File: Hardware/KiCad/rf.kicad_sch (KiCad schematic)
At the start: 29 parts, among them J8 Conn_Coaxial, U4 CC1200, Y3 40 MHz

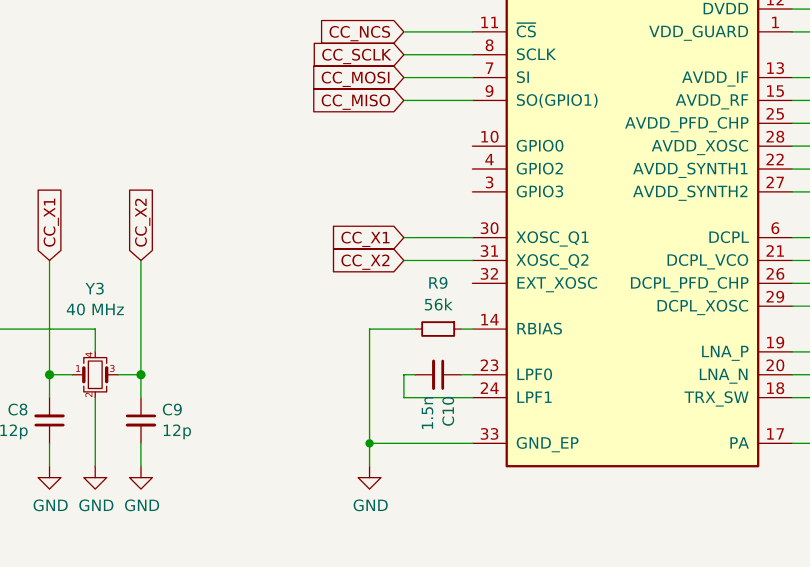
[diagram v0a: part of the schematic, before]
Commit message: Add decoupling capacitors and fix issue #7
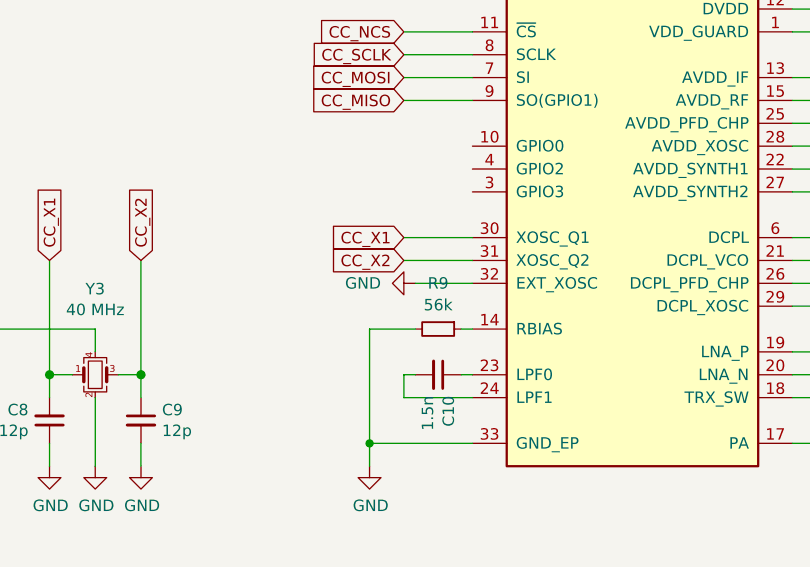
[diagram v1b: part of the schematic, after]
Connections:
- net GND: now also U4.32 (EXT_XOSC)
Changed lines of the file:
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@@
+    (stroke (width 0) (type default) (color 0 0 0 0))
+  )
+  (wire (pts (xy 86.36 63.5) (xy 92.71 63.5))
     (stroke (width 0) (type default) (color 0 0 0 0))
   )
@@
       (effects (font (size 1.27 1.27)) hide)
     )
+    (pin "1")
+  )
+  (symbol (lib_id "power:GND") (at 86.36 63.5 270) (unit 1)
+    (in_bom yes) (on_board yes) (fields_autoplaced)
+    (property "Reference" "#PWR014" (id 0) (at 80.01 63.5 0)
+      (effects (font (size 1.27 1.27)) hide)
+    )
+    (property "Value" "GND" (id 1) (at 82.55 63.4999 90)
+      (effects (font (size 1.27 1.27)) (justify right))
+    )
+    (property "Footprint" "" (id 2) (at 86.36 63.5 0)
+      (effects (font (size 1.27 1.27)) hide)
+    )
+    (property "Datasheet" "" (id 3) (at 86.36 63.5 0)
+      (effects (font (size 1.27 1.27)) hide)
+    )

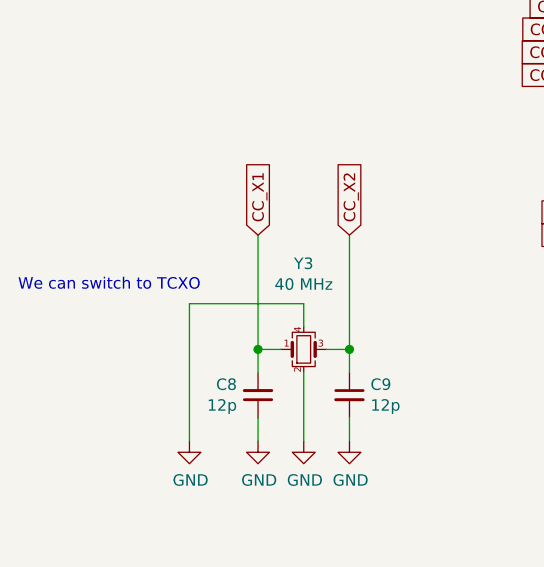
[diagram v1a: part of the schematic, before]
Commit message: Added footprints for decoupling caps
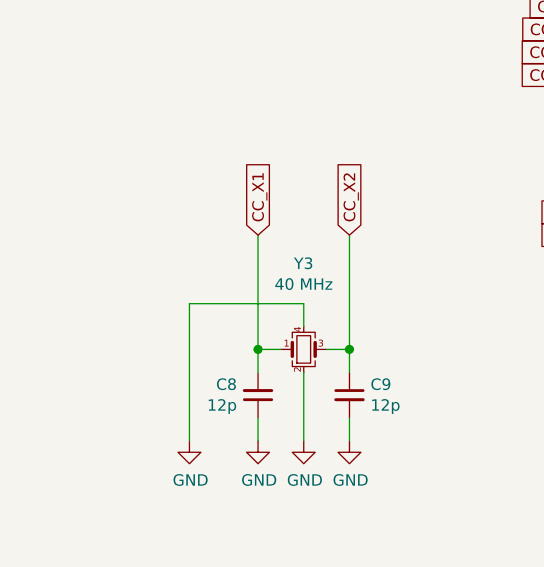
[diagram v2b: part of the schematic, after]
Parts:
- J8: footprint (none) -> Connector_Coaxial:SMA_Amphenol_901-143_Horizontal
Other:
- note removed: "We can switch to TCXO"
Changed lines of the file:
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@@
     (stroke (width 0) (type default) (color 0 0 0 0))
-  )
-  (text "We can switch to TCXO" (at 19.05 67.31 0)
-    (effects (font (size 1.27 1.27)) (justify left bottom))
   )
   (text "Add 9 (?) caps here" (at 139.7 26.67 0)
@@
       (effects (font (size 1.27 1.27)) (justify left))
     )
-    (property "Footprint" "" (id 2) (at 148.59 132.08 0)
-      (effects (font (size 1.27 1.27)) hide)
-    )
+    (property "Footprint" "Connector_Coaxial:SMA_Amphenol_901-143_Horizontal" (id 2) (at 148.59 132.08 0)
+      (effects (font (size 1.27 1.27)) hide)
+    )

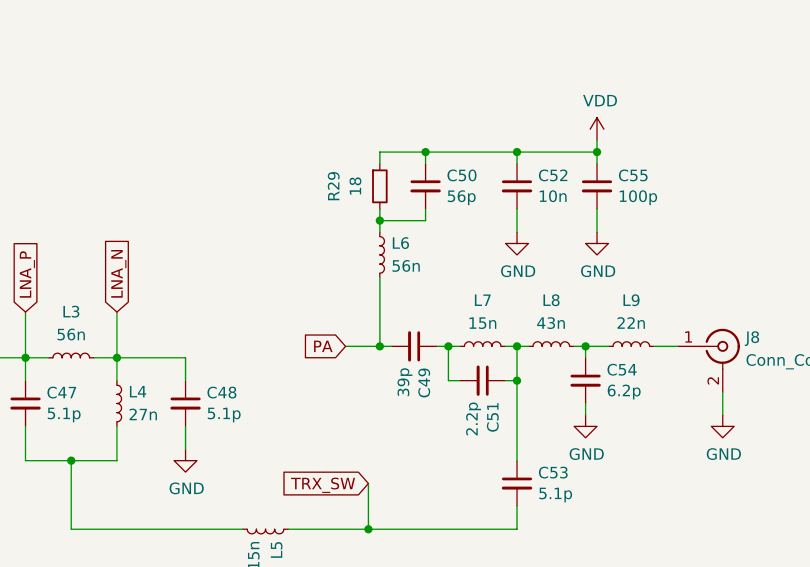
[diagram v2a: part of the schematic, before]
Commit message: Connected SD card to the micro
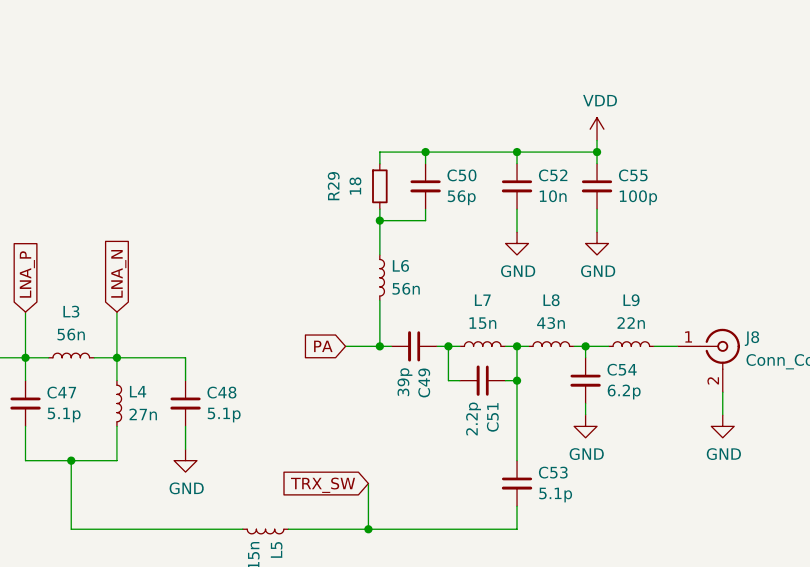
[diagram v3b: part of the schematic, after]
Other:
- moved on the sheet: L6
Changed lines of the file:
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@@
     (stroke (width 0) (type default) (color 0 0 0 0))
   )
-  (wire (pts (xy 110.49 124.46) (xy 110.49 132.08))
+  (wire (pts (xy 110.49 127) (xy 110.49 132.08))
     (stroke (width 0) (type default) (color 0 0 0 0))
   )
@@
     (stroke (width 0) (type default) (color 0 0 0 0))
   )
-  (wire (pts (xy 110.49 118.11) (xy 110.49 119.38))
+  (wire (pts (xy 110.49 118.11) (xy 110.49 121.92))
     (stroke (width 0) (type default) (color 0 0 0 0))
   )
@@
     (pin "1")
   )
-  (symbol (lib_id "Device:L_Small") (at 110.49 121.92 0) (unit 1)
+  (symbol (lib_id "Device:L_Small") (at 110.49 124.46 0) (unit 1)
     (in_bom yes) (on_board yes) (fields_autoplaced)
-    (property "Reference" "L6" (id 0) (at 111.76 120.6499 0)
-      (effects (font (size 1.27 1.27)) (justify left))
-    )
-    (property "Value" "56n" (id 1) (at 111.76 123.1899 0)
-      (effects (font (size 1.27 1.27)) (justify left))
-    )
-    (property "Footprint" "Inductor_SMD:L_0402_1005Metric" (id 2) (at 110.49 121.92 0)
-      (effects (font (size 1.27 1.27)) hide)
-    )
-    (property "Datasheet" "~" (id 3) (at 110.49 121.92 0)
-      (effects (font (size 1.27 1.27)) hide)
-    )
+    (property "Reference" "L6" (id 0) (at 111.76 123.1899 0)
+      (effects (font (size 1.27 1.27)) (justify left))
+    )
+    (property "Value" "56n" (id 1) (at 111.76 125.7299 0)
+      (effects (font (size 1.27 1.27)) (justify left))
+    )
+    (property "Footprint" "Inductor_SMD:L_0402_1005Metric" (id 2) (at 110.49 124.46 0)
+      (effects (font (size 1.27 1.27)) hide)
+    )
+    (property "Datasheet" "~" (id 3) (at 110.49 124.46 0)
+      (effects (font (size 1.27 1.27)) hide)
+    )

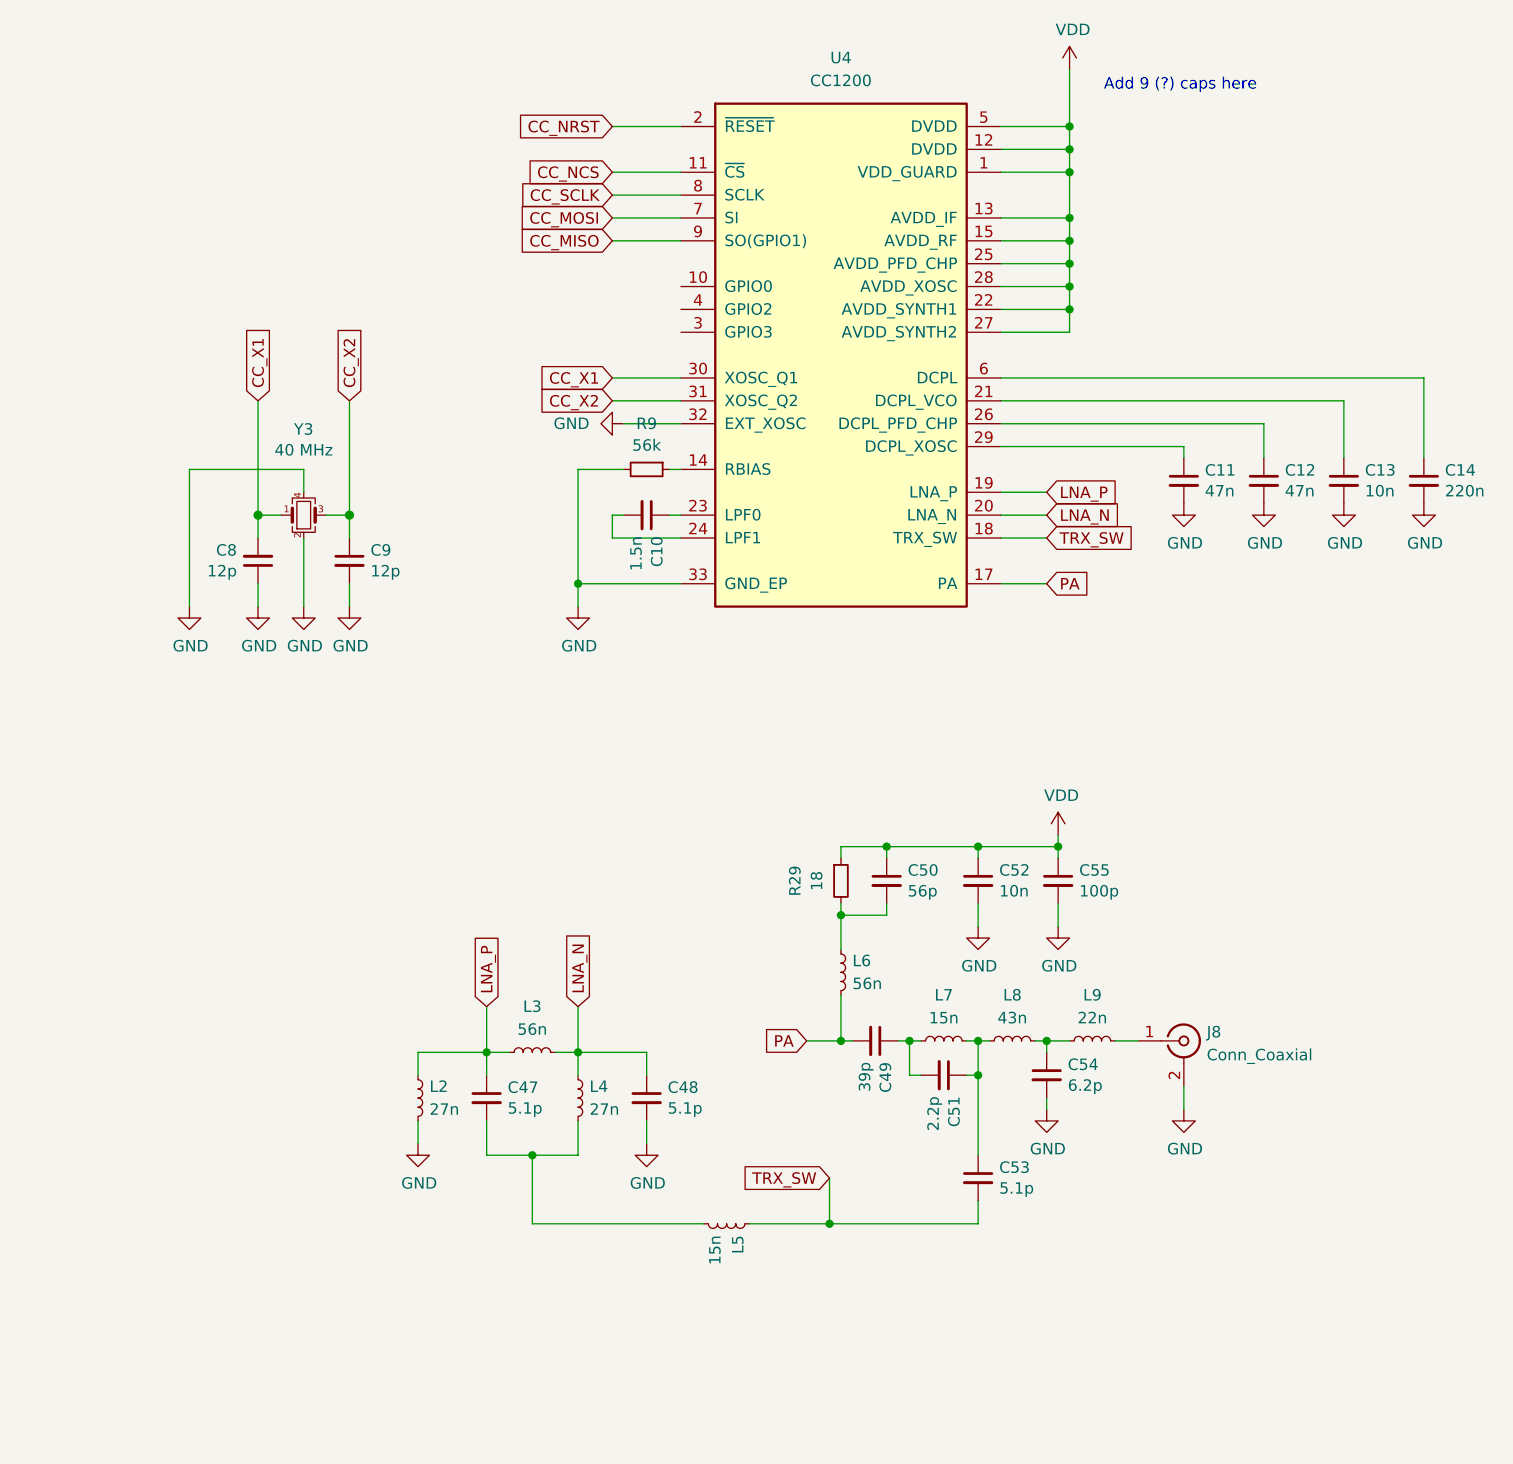
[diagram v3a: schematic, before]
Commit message: Added some connections
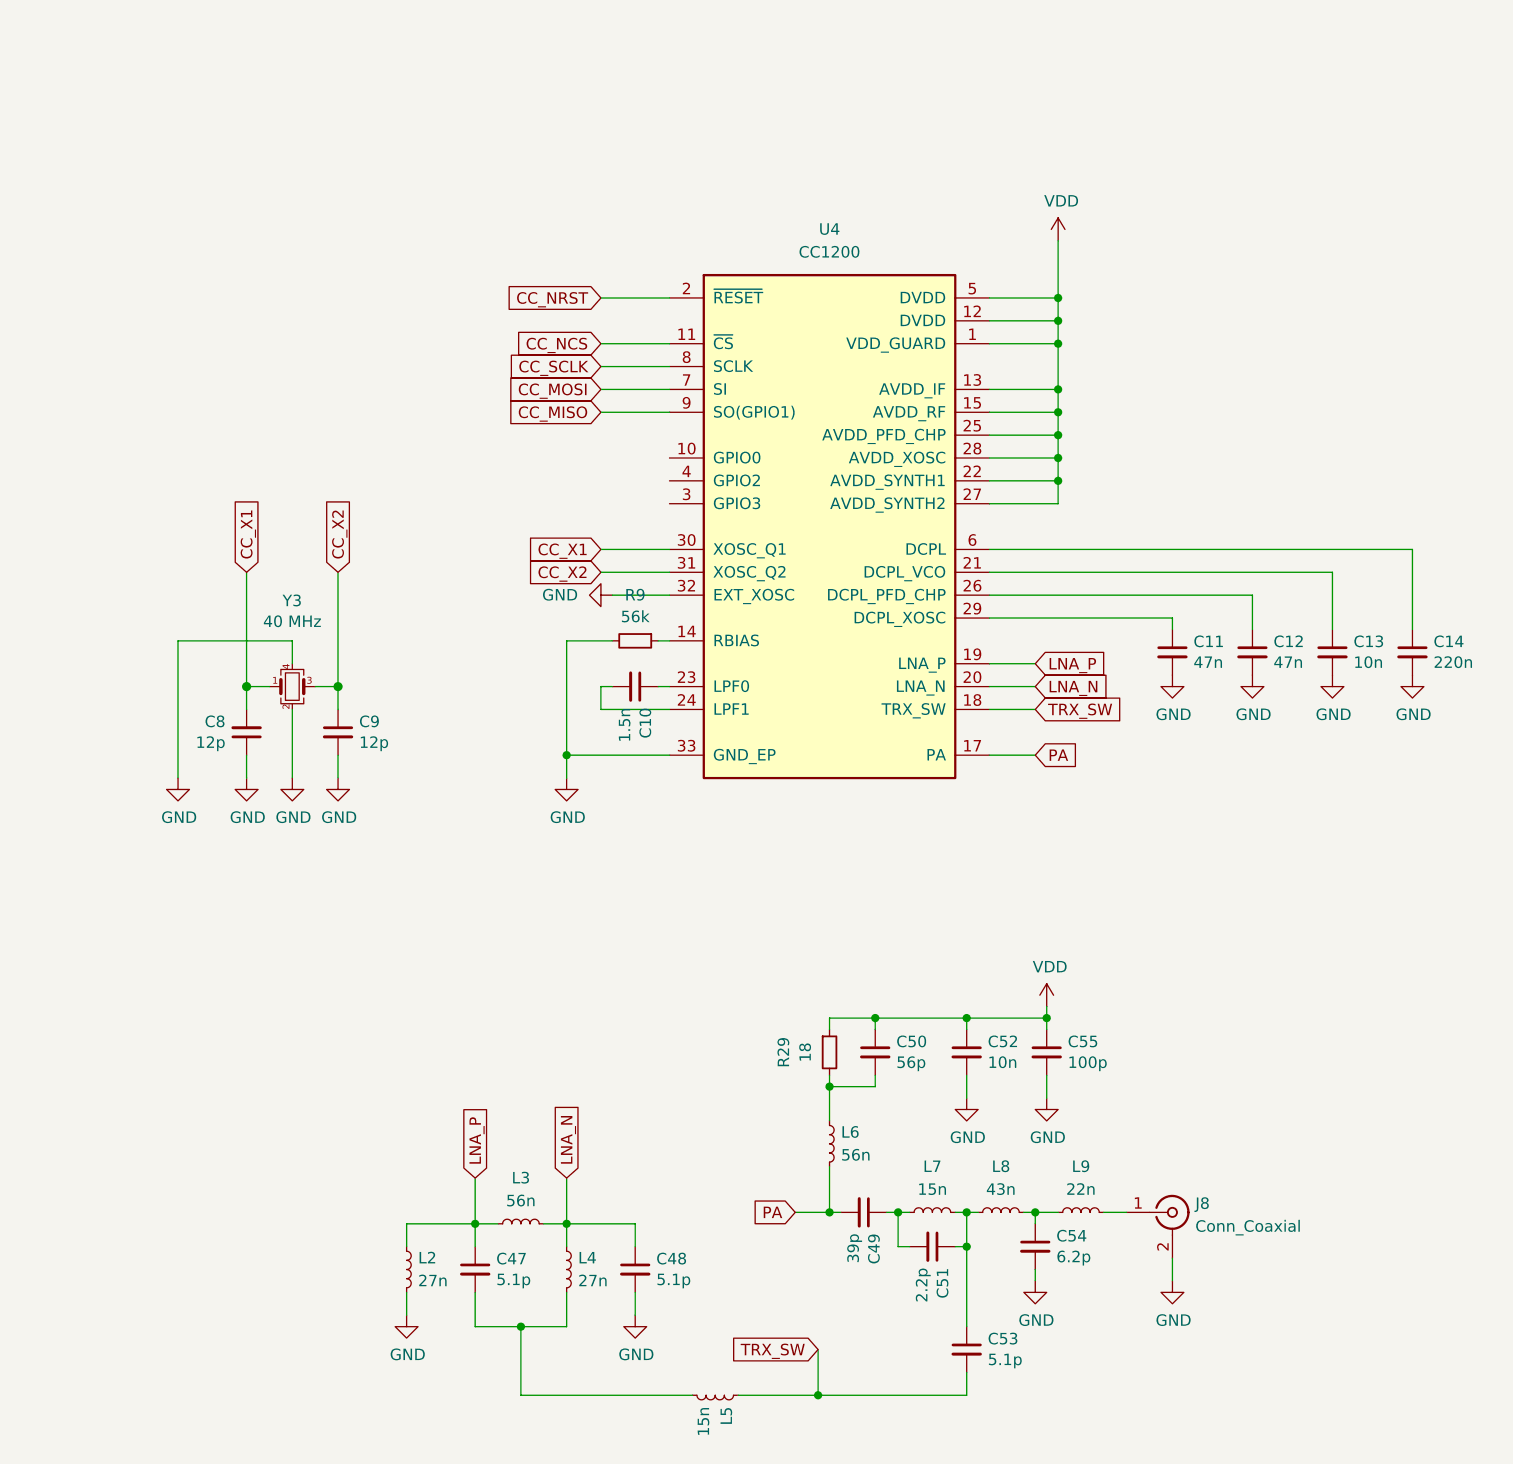
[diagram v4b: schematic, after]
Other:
- note removed: "Add 9 (?) caps here"
- moved on the sheet: C10, C11, C12, C13, C14, C47, C48, C49, C50, C51, C52, C53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

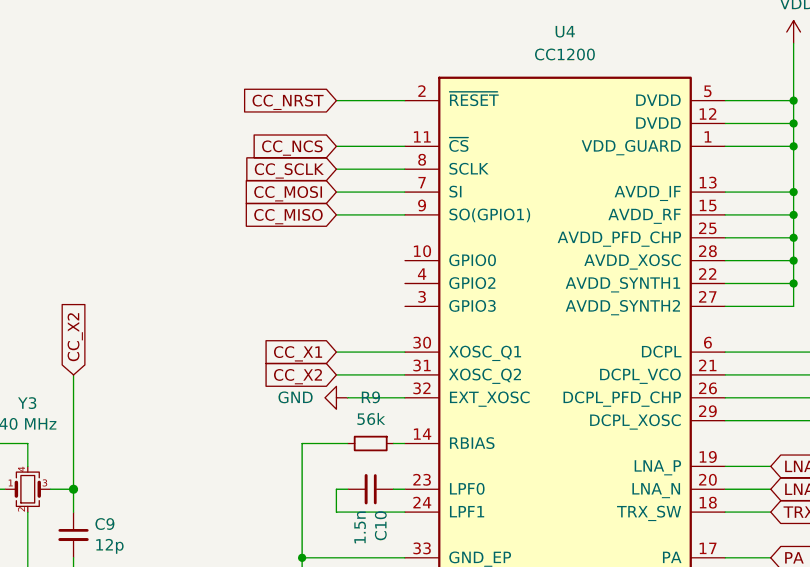
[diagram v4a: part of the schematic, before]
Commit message: Add no connection labels, anotate schematic, regen pdf and create netlist
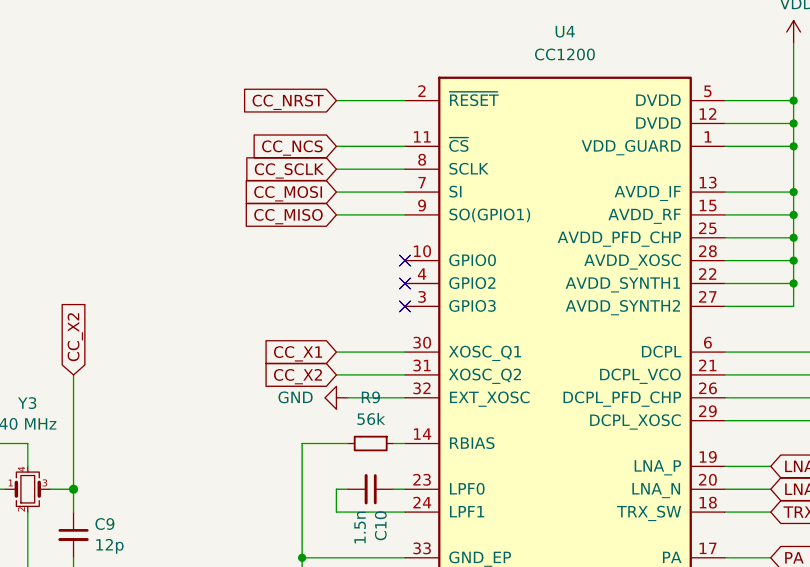
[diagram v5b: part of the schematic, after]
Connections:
- no-connect marks 0 -> 3
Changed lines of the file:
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@@
   (junction (at 44.45 92.71) (diameter 1.016) (color 0 0 0 0)
   )
+  (no_connect (at 91.44 67.31))
+  (no_connect (at 91.44 69.85))
+  (no_connect (at 91.44 72.39))
   (wire (pts (xy 134.62 54.61) (xy 134.62 59.69))
     (stroke (width 0) (type default) (color 0 0 0 0))
